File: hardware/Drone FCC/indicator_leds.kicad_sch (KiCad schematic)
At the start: 50 parts, among them Q1101 2N7002, Q1102 2N7002, Q1103 2N7002, Q1104 2N7002, Q1105 2N7002, Q1106 2N7002, Q1107 2N7002, Q1108 2N7002, SW1101 SW Proposito General, SW1102 SW Proposito General

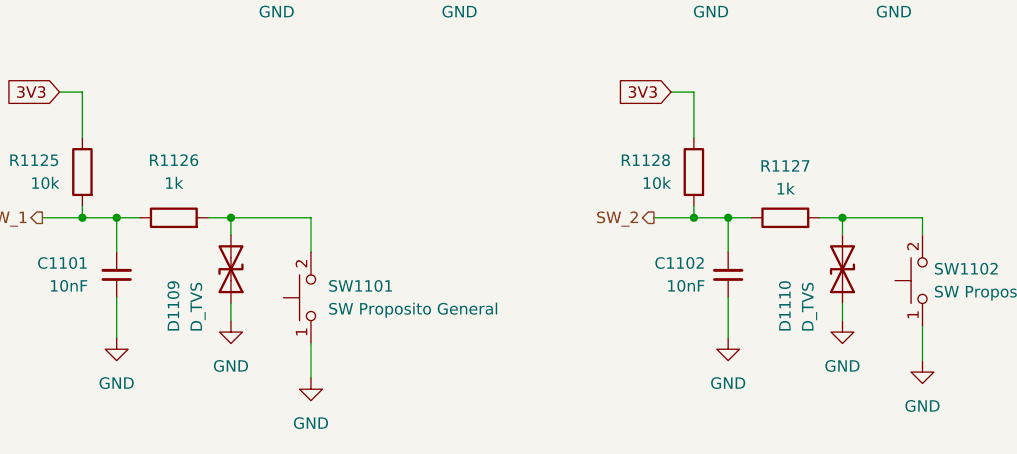
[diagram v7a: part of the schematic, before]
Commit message: removed all the TVS from the PCB and SCH
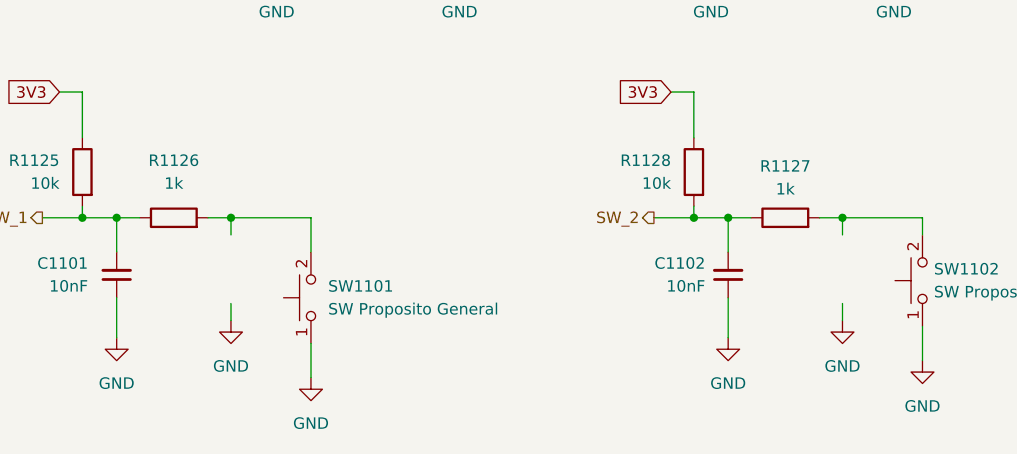
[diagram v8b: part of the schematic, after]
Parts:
- removed D1109, D1110: D_TVS, Diode_SMD:D_0402_1005Metric_Pad0.77x0.64mm_HandSolder, symbol Device:D_TVS
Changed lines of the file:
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@@
     (pin "1")
-  )
-  (symbol (lib_id "Device:D_TVS") (at 110.49 173.355 270) (mirror x) (unit 1)
-    (in_bom yes) (on_board yes)
-    (property "Reference" "D1110" (id 0) (at 104.14 180.34 0)
-      (effects (font (size 1.27 1.27)) (justify left))
-    )
-    (property "Value" "D_TVS" (id 1) (at 106.68 180.34 0)
-      (effects (font (size 1.27 1.27)) (justify left))
-    )
-    (property "Footprint" "Diode_SMD:D_0402_1005Metric_Pad0.77x0.64mm_HandSolder" (id 2) (at 110.49 173.355 0)
-      (effects (font (size 1.27 1.27)) hide)
-    )
-    (property "Datasheet" "~" (id 3) (at 110.49 173.355 0)
-      (effects (font (size 1.27 1.27)) hide)
-    )
-    (pin "1")
-    (pin "2")
   )
   (symbol (lib_id "Device:C_Small") (at 29.845 173.99 0) (mirror x) (unit 1)
@@
       (effects (font (size 1.27 1.27)) hide)
     )
-    (pin "1")
-    (pin "2")
-  )
-  (symbol (lib_id "Device:D_TVS") (at 42.545 173.355 270) (mirror x) (unit 1)
-    (in_bom yes) (on_board yes)
-    (property "Reference" "D1109" (id 0) (at 36.195 180.34 0)
-      (effects (font (size 1.27 1.27)) (justify left))
-    )
-    (property "Value" "D_TVS" (id 1) (at 38.735 180.34 0)
-      (effects (font (size 1.27 1.27)) (justify left))
-    )
-    (property "Footprint" "Diode_SMD:D_0402_1005Metric_Pad0.77x0.64mm_HandSolder" (id 2) (at 42.545 173.355 0)
-      (effects (font (size 1.27 1.27)) hide)
-    )
-    (property "Datasheet" "~" (id 3) (at 42.545 173.355 0)
-      (effects (font (size 1.27 1.27)) hide)
-    )
